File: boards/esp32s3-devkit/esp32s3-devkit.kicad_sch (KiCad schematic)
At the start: 37 parts, among them J1 Conn_01x17_Pin, J2 Conn_01x17_Pin, J3 USB_C_Receptacle_USB2.0_14P, Q1 Q_PMOS_GSD, SW1 ON/OFF, SW2 RESET, SW3 BOOT, U1 TPS630701RNMR, U2 ESP32-S3-WROOM-1, U3 USBLC6-2SC6

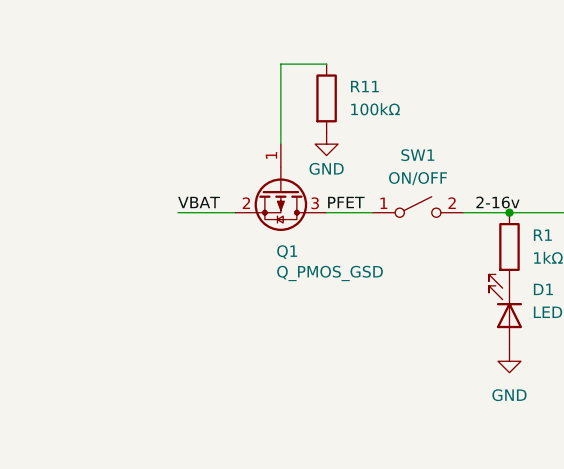
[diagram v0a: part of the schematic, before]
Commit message: fix(esp32s3-devkit): add PWR_FLAG on VBAT for ERC
Anchors KiCad ERC to the incoming supply net and keeps pcb/pro synced with schematic.
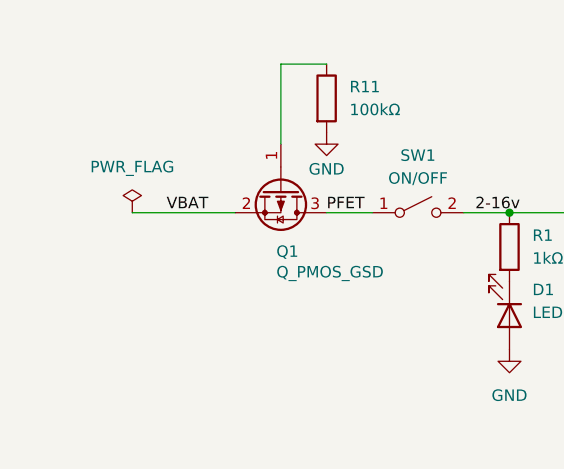
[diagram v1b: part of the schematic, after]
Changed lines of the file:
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@@
 	(wire
 		(pts
-			(xy 35.56 46.99) (xy 41.91 46.99)
+			(xy 30.48 46.99) (xy 41.91 46.99)
 		)
 		(stroke
@@
 		)
 	)
-	(label "GPIO48"
-		(at 231.14 121.92 0)
+	(label "VBAT"
+		(at 34.29 46.99 0)
 		(effects
 			(font
@@
 		)
 	)
-	(label "GPIO15"
-		(at 262.89 138.43 0)
+	(label "GPIO48"
+		(at 231.14 121.92 0)
 		(effects
 			(font
@@
 		)
 	)
-	(label "VBAT"
-		(at 35.56 46.99 0)
+	(label "GPIO15"
+		(at 262.89 138.43 0)
 		(effects
 			(font
@@
 					(unit 1)
 				)
+			)
+		)
+	)
+	(symbol
+		(lib_id "power:PWR_FLAG")
+		(at 30.48 46.99 0)
+		(unit 1)
+		(body_style 1)
+		(exclude_from_sim no)
+		(in_bom yes)
+		(on_board yes)
+		(in_pos_files yes)
+		(dnp no)
+		(fields_autoplaced yes)
+		(property "Reference" "#FLG01"
+			(at 30.48 45.085 0)
+			(hide yes)
+			(show_name no)
+			(do_not_autoplace no)
+			(effects
+				(font
+					(size 1.27 1.27)
+				)
+			)
+		)
+		(property "Value" "PWR_FLAG"
+			(at 30.48 41.91 0)
+			(show_name no)
+			(do_not_autoplace no)
+			(effects
+				(font
+					(size 1.27 1.27)
+				)
+			)
+		)
+		(property "Footprint" ""
+			(at 30.48 46.99 0)
+			(hide yes)
+			(show_name no)
+			(do_not_autoplace no)
+			(effects
+				(font
+					(size 1.27 1.27)
+				)
+			)
+		)
+		(property "Datasheet" ""
+			(at 30.48 46.99 0)
+			(hide yes)
+			(show_name no)
+			(do_not_autoplace no)
+			(effects
+				(font
+					(size 1.27 1.27)
+				)
+			)
+		)
+		(property "Description" "Special symbol for telling ERC where power comes from"
+			(at 30.48 46.99 0)
+			(hide yes)
+			(show_name no)
+			(do_not_autoplace no)
+			(effects
+				(font
+					(size 1.27 1.27)
+				)
+			)
+		)
+		(pin "1"
+		)
+		(instances
+			(project "esp32s3-devkit"
+				(path "/7924bd8b-2498-4d76-899d-c0ad5a514485"
+					(reference "#FLG01")
+					(unit 1)
+				)

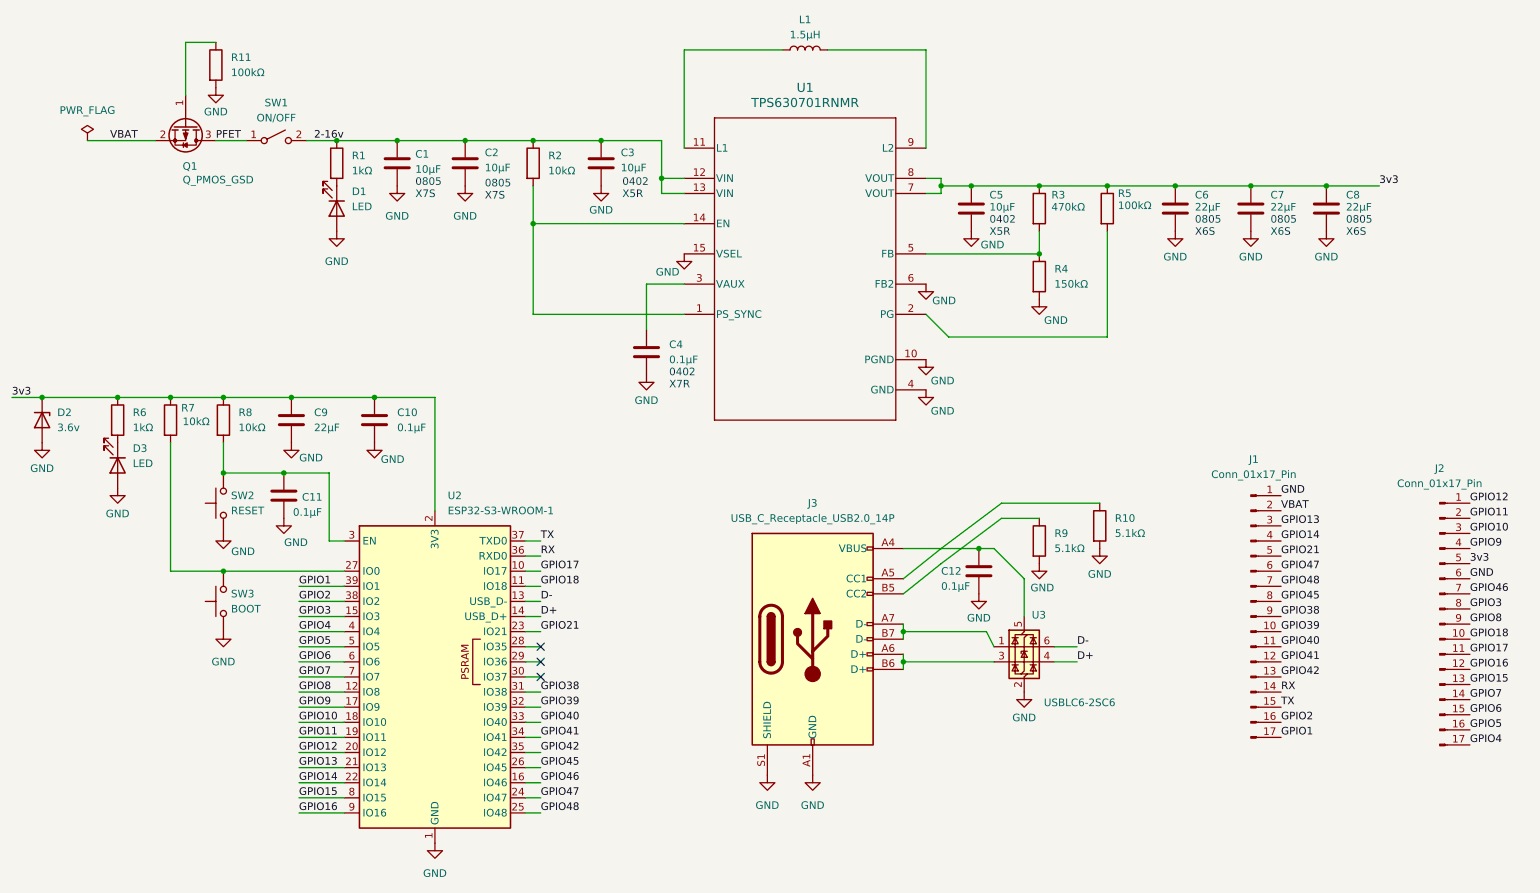
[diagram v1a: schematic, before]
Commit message: fix(esp32s3-devkit): add ERC PWR_FLAGS on remaining supply nets
Adds additional PWR_FLAG instances and rewires schematic so KiCad ERC sees explicit power sources alongside GND anchors.
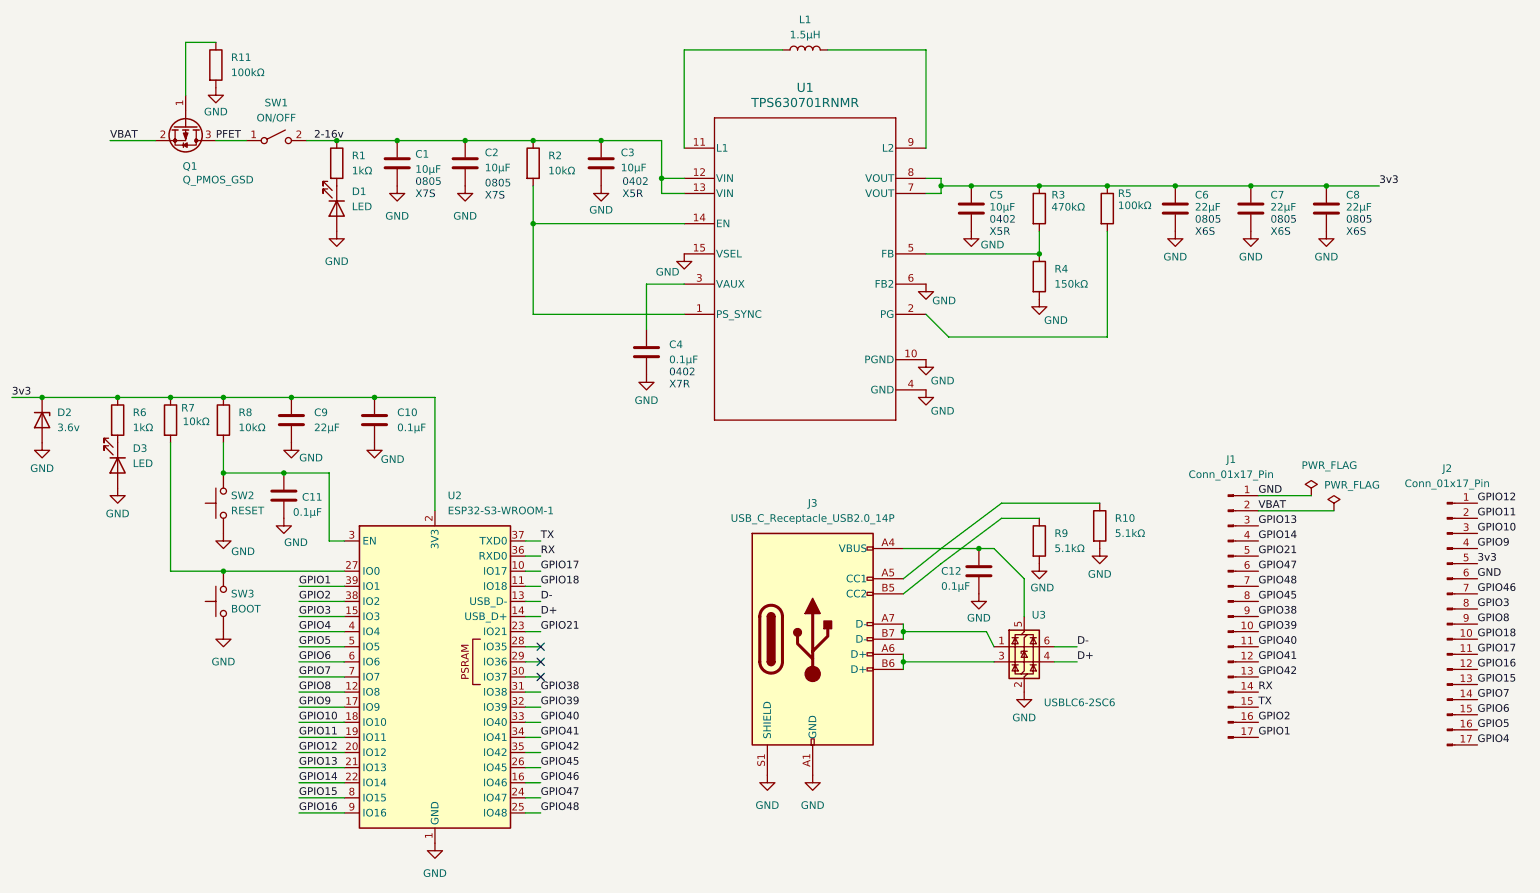
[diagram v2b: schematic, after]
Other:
- moved on the sheet: J1, J2

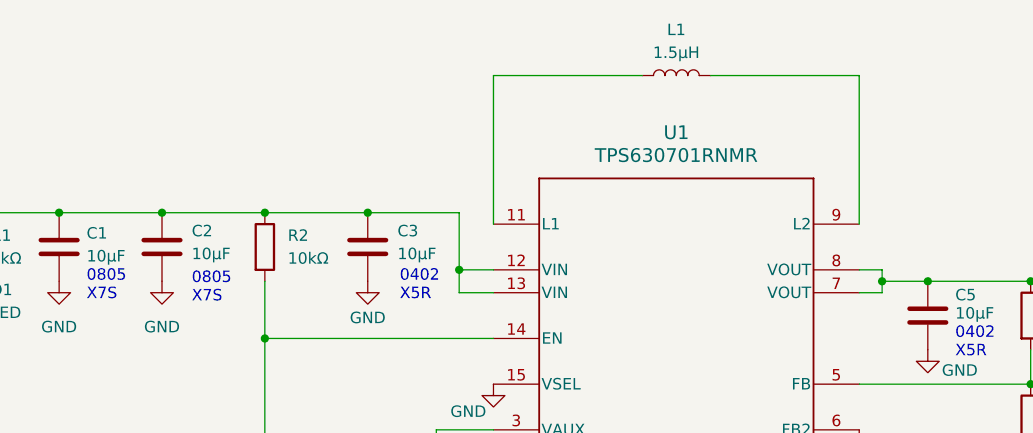
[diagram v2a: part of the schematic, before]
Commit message: fix(esp32s3-devkit): resolve TPS630701/USB ERC (PWR + symbol pin types)
- Add PWR_FLAG on the `2-16v` regulator input net (past the OR-ing) and align embedded TPS630701 with libs/symbols (VOUT/power pins, SIM props).
- Quote USB-C footprint as Connector_USB:* on J3 so KiCad resolves the nickname.
- Silence `lib_symbol_mismatch` in project ERC severities until embedded Connector artwork matches stock (KiCad cosmetic/stroke deltas only).
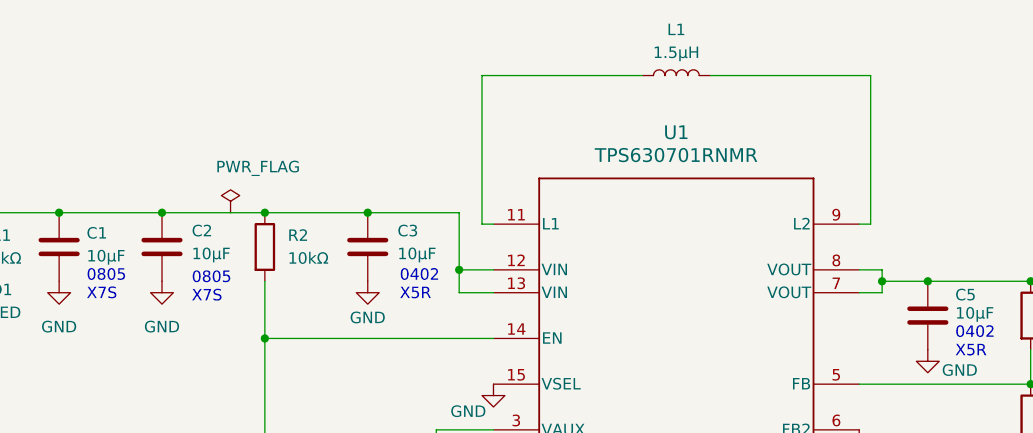
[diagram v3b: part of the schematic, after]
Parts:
- J3: footprint USB_C_Receptacle_HRO_TYPE-C-31-M-12 -> Connector_USB:USB_C_Receptacle_HRO_TYPE-C-31-M-12
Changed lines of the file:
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@@
 	(wire
 		(pts
+			(xy 171.45 48.26) (xy 172.72 48.26)
+		)
+		(stroke
+			(width 0)
+			(type default)
+		)
+	)
+	(wire
+		(pts
 			(xy 167.64 129.54) (xy 167.64 130.81)
 		)
@@
 	(wire
 		(pts
-			(xy 171.45 31.75) (xy 171.45 48.26)
-		)
-		(stroke
-			(width 0)
-			(type default)
-		)
-	)
-	(wire
-		(pts
 			(xy 104.14 157.48) (xy 106.68 157.48)
 		)
@@
 	(wire
 		(pts
+			(xy 129.54 31.75) (xy 147.32 31.75)
+		)
+		(stroke
+			(width 0)
+			(type default)
+		)
+	)
+	(wire
+		(pts
 			(xy 201.93 54.61) (xy 213.36 54.61)
 		)
@@
 	(wire
 		(pts
-			(xy 154.94 31.75) (xy 171.45 31.75)
+			(xy 154.94 31.75) (xy 172.72 31.75)
 		)
 		(stroke
@@
 	(wire
 		(pts
-			(xy 130.81 31.75) (xy 130.81 48.26)
+			(xy 78.74 90.17) (xy 88.9 90.17)
 		)
 		(stroke
@@
 	(wire
 		(pts
-			(xy 78.74 90.17) (xy 88.9 90.17)
+			(xy 127 46.99) (xy 127 53.34)
 		)
 		(stroke
@@
 	(wire
 		(pts
-			(xy 127 46.99) (xy 127 53.34)
+			(xy 104.14 139.7) (xy 106.68 139.7)
 		)
 		(stroke
@@
 	(wire
 		(pts
-			(xy 104.14 139.7) (xy 106.68 139.7)
+			(xy 172.72 31.75) (xy 172.72 48.26)
+		)
+		(stroke
+			(width 0)
+			(type default)
+		)
+	)
+	(wire
+		(pts
+			(xy 129.54 48.26) (xy 130.81 48.26)
 		)
 		(stroke
@@
 	(wire
 		(pts
-			(xy 93.98 46.99) (xy 105.41 46.99)
+			(xy 93.98 46.99) (xy 101.6 46.99)
+		)
+		(stroke
+			(width 0)
+			(type default)
+		)
+	)
+	(wire
+		(pts
+			(xy 101.6 46.99) (xy 105.41 46.99)
 		)
 		(stroke
@@
 	(wire
 		(pts
-			(xy 130.81 31.75) (xy 147.32 31.75)
+			(xy 184.15 107.95) (xy 200.66 107.95)
 		)
 		(stroke
@@
 	(wire
 		(pts
-			(xy 184.15 107.95) (xy 200.66 107.95)
+			(xy 66.04 127) (xy 73.66 127)
 		)
 		(stroke
@@
 	(wire
 		(pts
-			(xy 66.04 127) (xy 73.66 127)
+			(xy 173.99 115.57) (xy 167.64 120.65)
 		)
 		(stroke
@@
 	(wire
 		(pts
-			(xy 173.99 115.57) (xy 167.64 120.65)
+			(xy 66.04 160.02) (xy 73.66 160.02)
 		)
 		(stroke
@@
 	(wire
 		(pts
-			(xy 66.04 160.02) (xy 73.66 160.02)
+			(xy 66.04 152.4) (xy 73.66 152.4)
 		)
 		(stroke
@@
 	(wire
 		(pts
-			(xy 66.04 152.4) (xy 73.66 152.4)
+			(xy 66.04 132.08) (xy 73.66 132.08)
 		)
 		(stroke
@@
 	(wire
 		(pts
-			(xy 66.04 132.08) (xy 73.66 132.08)
+			(xy 173.99 54.61) (xy 173.99 55.88)
 		)
 		(stroke
@@
 	(wire
 		(pts
-			(xy 173.99 54.61) (xy 173.99 55.88)
+			(xy 129.54 31.75) (xy 129.54 48.26)
 		)
 		(stroke
@@
 	(symbol
 		(lib_id "power:PWR_FLAG")
+		(at 101.6 46.99 0)
+		(unit 1)
+		(body_style 1)
+		(exclude_from_sim no)
+		(in_bom yes)
+		(on_board yes)
+		(in_pos_files yes)
+		(dnp no)
+		(property "Reference" "#FLG04"
+			(at 101.6 45.085 0)
+			(hide yes)
+			(show_name no)
+			(do_not_autoplace no)
+			(effects
+				(font
+					(size 1.27 1.27)
+				)
+			)
+		)
+		(property "Value" "PWR_FLAG"
+			(at 104.648 41.91 0)
+			(show_name no)
+			(do_not_autoplace no)
+			(effects
+				(font
+					(size 1.27 1.27)
+				)
+			)
+		)
+		(property "Footprint" ""
+			(at 101.6 46.99 0)
+			(hide yes)
+			(show_name no)
+			(do_not_autoplace no)
+			(effects
+				(font
+					(size 1.27 1.27)
+				)
+			)
+		)
+		(property "Datasheet" ""
+			(at 101.6 46.99 0)
+			(hide yes)
+			(show_name no)
+			(do_not_autoplace no)
+			(effects
+				(font
+					(size 1.27 1.27)
+				)
+			)
+		)
+		(property "Description" "Special symbol for telling ERC where power comes from"
+			(at 101.6 46.99 0)
+			(hide yes)
+			(show_name no)
+			(do_not_autoplace no)
+			(effects
+				(font
+					(size 1.27 1.27)
+				)
+			)
+		)
+		(pin "1"
+		)
+		(instances
+			(project "esp32s3-devkit"
+				(path "/7924bd8b-2498-4d76-899d-c0ad5a514485"
+					(reference "#FLG04")
+					(unit 1)
+				)
+			)
+		)
+	)
+	(symbol
+		(lib_id "power:PWR_FLAG")
 		(at 236.22 106.68 0)
 		(unit 1)
@@
 			)
 		)
-		(property "Footprint" "USB_C_Receptacle_HRO_TYPE-C-31-M-12"
+		(property "Footprint" "Connector_USB:USB_C_Receptacle_HRO_TYPE-C-31-M-12"
 			(at 156.21 130.81 0)
 			(hide yes)

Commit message: fix(esp32s3-devkit): align USB-C HRO footprint shield pads with schematic S1
Fork Connector_USB footprint into libs: rename mounting pads SH→S1 so
USB_C_Receptacle_USB2.0_14P links cleanly; register HRO_TypeC_USB in fp-lib-table
and refresh embedded pcb pads after reassignment.

SBU pads A8/B8 remain optional for a future move to USB2.0_16P + no-connect SBUs.
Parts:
- J3: footprint Connector_USB:USB_C_Receptacle_HRO_TYPE-C-31-M-12 -> HRO_TypeC_USB:USB_C_Receptacle_HRO_TYPE-C-31-M-12
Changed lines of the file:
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@@
 			)
 		)
-		(property "Footprint" "Connector_USB:USB_C_Receptacle_HRO_TYPE-C-31-M-12"
+		(property "Footprint" "HRO_TypeC_USB:USB_C_Receptacle_HRO_TYPE-C-31-M-12"
 			(at 156.21 130.81 0)
 			(hide yes)
